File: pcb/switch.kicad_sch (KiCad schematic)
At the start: 2 parts, among them J2 Conn_01x02_Pin, Q6 AO3400A

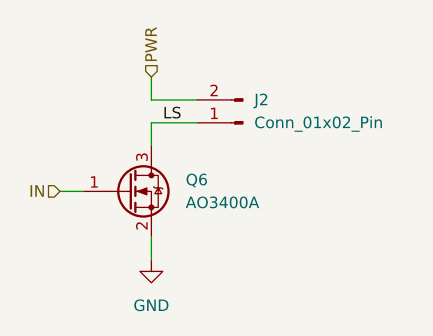
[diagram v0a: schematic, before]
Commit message: Finish schematic
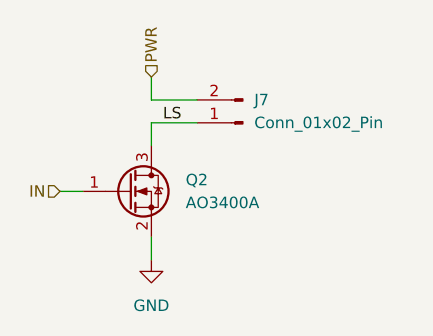
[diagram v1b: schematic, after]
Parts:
- renumbered J2 to J7, Q6 to Q2
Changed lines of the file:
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@@
 		(dnp no)
 		(fields_autoplaced yes)
-		(property "Reference" "Q6"
+		(property "Reference" "Q2"
 			(at 105.41 67.3099 0)
 			(effects
@@
 		(dnp no)
 		(fields_autoplaced yes)
-		(property "Reference" "J2"
+		(property "Reference" "J7"
 			(at 113.03 58.4199 0)
 			(effects
@@
 			(project "raven"
 				(path "/38b0a34b-2047-47f6-90d7-ccdf77e8e212/7e3f67f4-c7a7-4f15-a62c-4903c0d88b19/0468a395-528f-40e9-a80c-ea76604d83d5"
-					(reference "J3")
+					(reference "J7")
 					(unit 1)
 				)
 				(path "/38b0a34b-2047-47f6-90d7-ccdf77e8e212/7e3f67f4-c7a7-4f15-a62c-4903c0d88b19/342a8149-844d-48b1-b606-577c49d96b64"
-					(reference "J5")
+					(reference "J9")
 					(unit 1)
 				)
 				(path "/38b0a34b-2047-47f6-90d7-ccdf77e8e212/7e3f67f4-c7a7-4f15-a62c-4903c0d88b19/389c9745-b4ed-4a72-983a-3e20800a0a90"
-					(reference "J13")
+					(reference "J20")
 					(unit 1)
 				)
 				(path "/38b0a34b-2047-47f6-90d7-ccdf77e8e212/7e3f67f4-c7a7-4f15-a62c-4903c0d88b19/6efef10c-3fe0-4055-829d-9b7a714ef2a6"
-					(reference "J2")
+					(reference "J6")
 					(unit 1)
 				)
 				(path "/38b0a34b-2047-47f6-90d7-ccdf77e8e212/7e3f67f4-c7a7-4f15-a62c-4903c0d88b19/907212ed-04bc-4847-9304-636cf67f996f"
-					(reference "J4")
+					(reference "J8")
 					(unit 1)
 				)
 				(path "/38b0a34b-2047-47f6-90d7-ccdf77e8e212/7e3f67f4-c7a7-4f15-a62c-4903c0d88b19/a6b29ecb-c69a-4a56-96a2-a4702bce8bfa"
-					(reference "J6")
+					(reference "J10")
 					(unit 1)
 				)
@@
 		(dnp no)
 		(fields_autoplaced yes)
-		(property "Reference" "#PWR0208"
+		(property "Reference" "#PWR025"
 			(at 101.6 82.55 0)
 			(effects
@@
 			(project "raven"
 				(path "/38b0a34b-2047-47f6-90d7-ccdf77e8e212/7e3f67f4-c7a7-4f15-a62c-4903c0d88b19/0468a395-528f-40e9-a80c-ea76604d83d5"
-					(reference "#PWR09")
+					(reference "#PWR025")
 					(unit 1)
 				)
 				(path "/38b0a34b-2047-47f6-90d7-ccdf77e8e212/7e3f67f4-c7a7-4f15-a62c-4903c0d88b19/342a8149-844d-48b1-b606-577c49d96b64"
-					(reference "#PWR011")
+					(reference "#PWR027")
 					(unit 1)
 				)
 				(path "/38b0a34b-2047-47f6-90d7-ccdf77e8e212/7e3f67f4-c7a7-4f15-a62c-4903c0d88b19/389c9745-b4ed-4a72-983a-3e20800a0a90"
-					(reference "#PWR0208")
+					(reference "#PWR0250")
 					(unit 1)
 				)
 				(path "/38b0a34b-2047-47f6-90d7-ccdf77e8e212/7e3f67f4-c7a7-4f15-a62c-4903c0d88b19/6efef10c-3fe0-4055-829d-9b7a714ef2a6"
-					(reference "#PWR08")
+					(reference "#PWR024")
 					(unit 1)
 				)
 				(path "/38b0a34b-2047-47f6-90d7-ccdf77e8e212/7e3f67f4-c7a7-4f15-a62c-4903c0d88b19/907212ed-04bc-4847-9304-636cf67f996f"
-					(reference "#PWR010")
+					(reference "#PWR026")
 					(unit 1)
 				)
 				(path "/38b0a34b-2047-47f6-90d7-ccdf77e8e212/7e3f67f4-c7a7-4f15-a62c-4903c0d88b19/a6b29ecb-c69a-4a56-96a2-a4702bce8bfa"
-					(reference "#PWR012")
-					(unit 1)
-				)
+					(reference "#PWR028")
+					(unit 1)
+				)
